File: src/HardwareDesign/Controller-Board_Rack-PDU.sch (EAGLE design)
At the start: 131 parts, among them IC2 RP2040, IC3 MCP6001, IC5 MIC5504-3.3YM5-TR, IC7 MP2315TSOT23-8, X1 25MHz, X2 12MHz

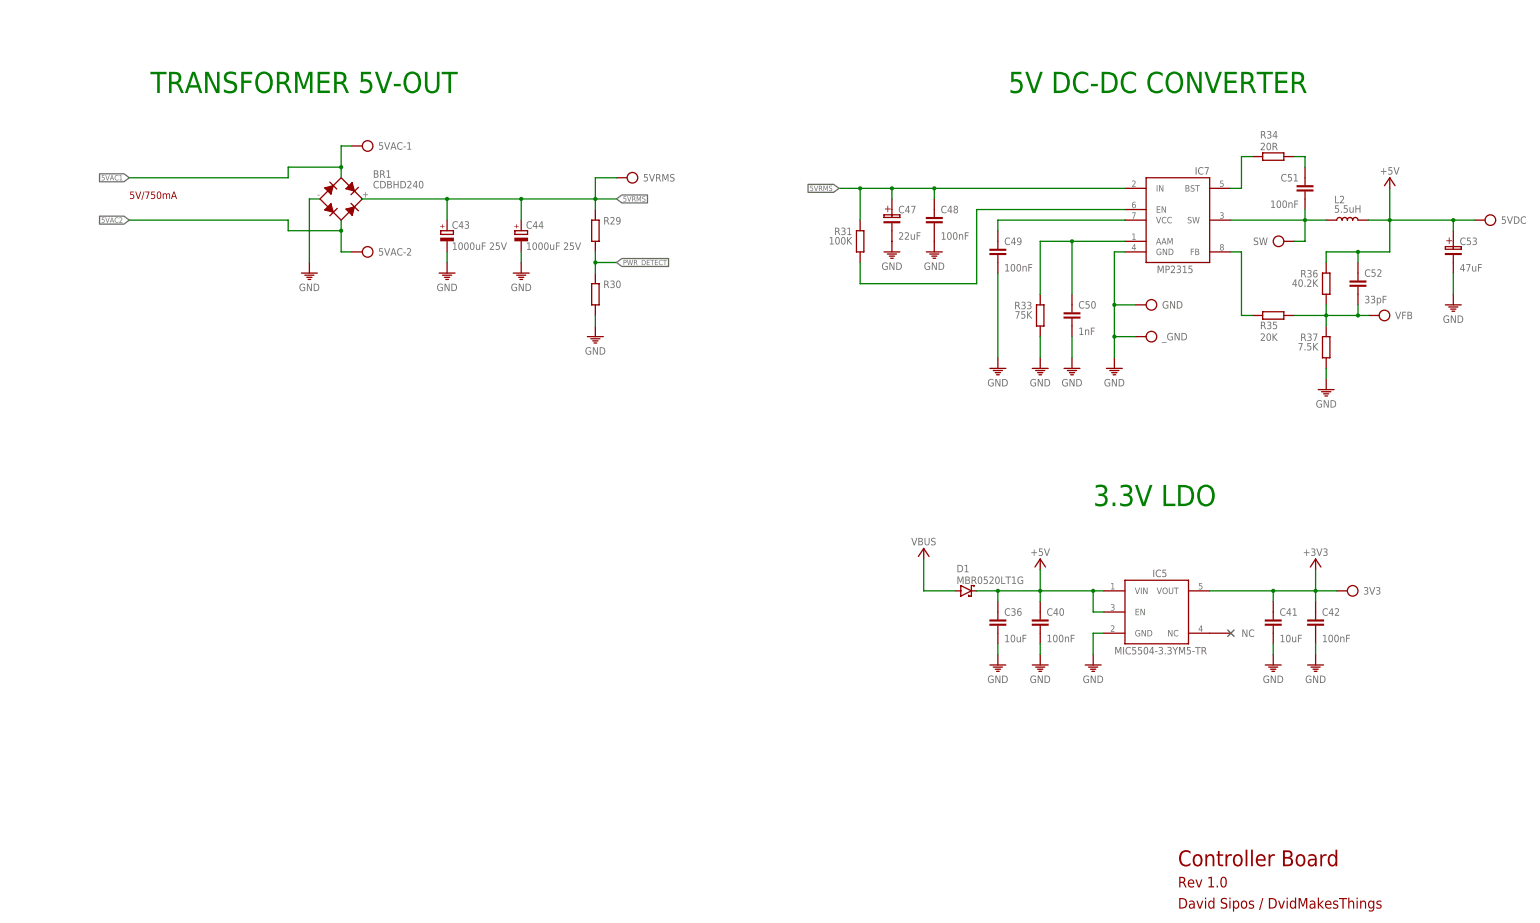
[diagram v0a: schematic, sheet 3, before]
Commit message: finish relay board design
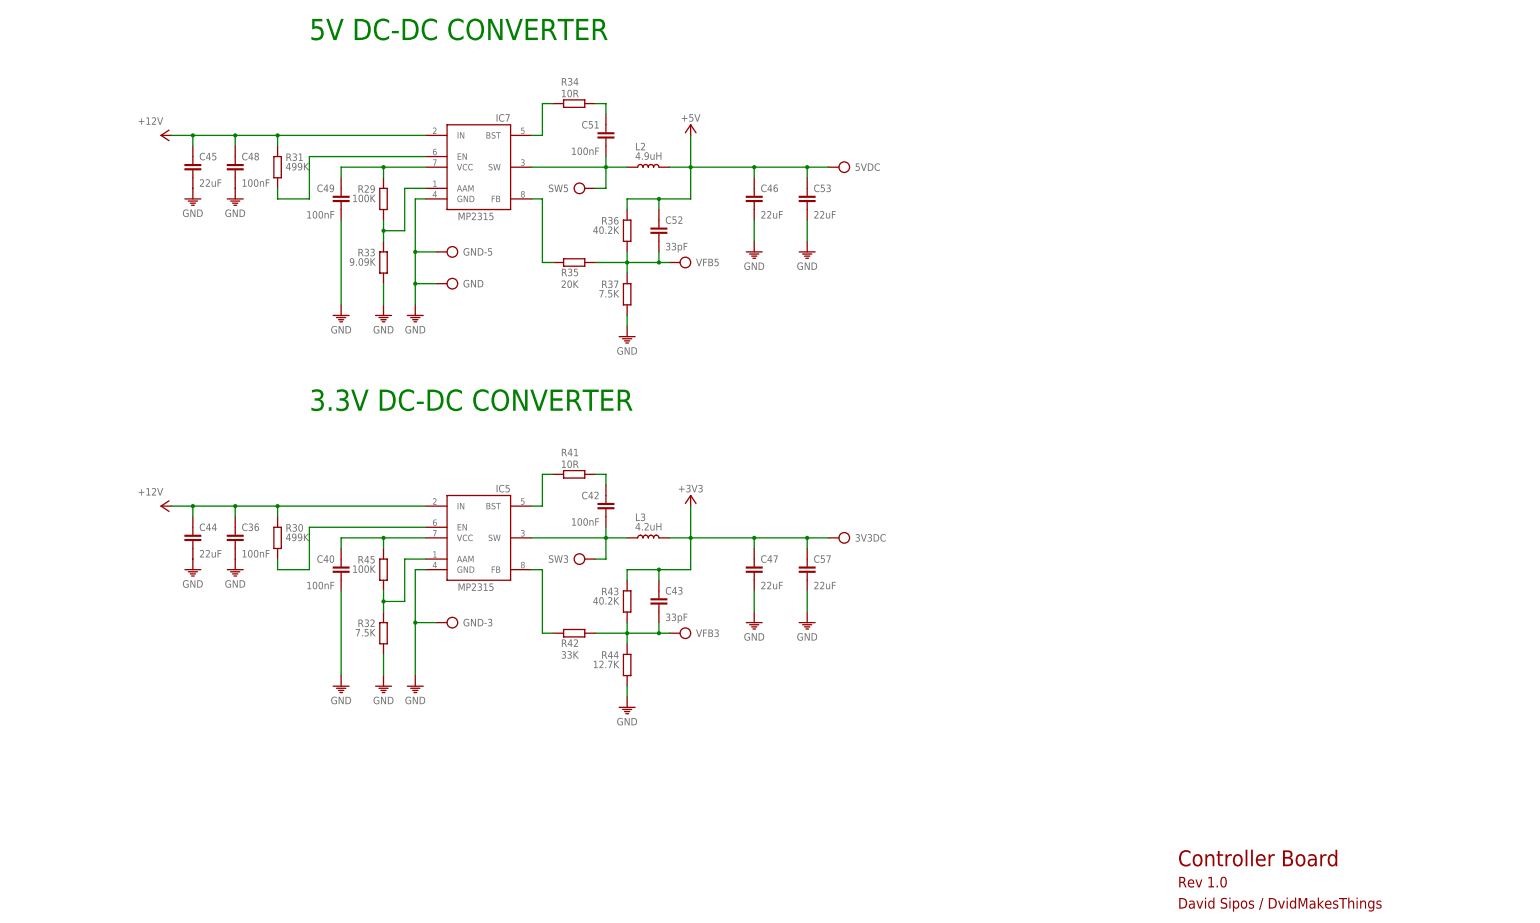
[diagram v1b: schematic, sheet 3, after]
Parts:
- removed 3V3, 5VAC-1, 5VAC-2, 5VRMS, SW, VFB, _GND: TP, ds_passive:TP
- removed BR1: CDBHD240, 52101-101-REV-A_v16:RECTIFIER_CDBHD240
- removed C41: 10uF, ds_passive:C0402
- removed C50: 1nF, ds_passive:C0402
- removed D1: MBR0520LT1G, Diodes:MBR0520LT1G
- added 12VFB, 3V3DC, GND-3, GND-5, SW3, SW5, VFB3, VFB5: TP, ds_passive:TP
- added C45, C46, C57: 22uF, ds_passive:C-1206
- added L3: 4.2uH, ds_passive:L
- added R32: 7.5K, ds_passive:R0402
- added R41: 10R, ds_passive:R0402
- added R42: 33K, ds_passive:R0402
- added R43: 40.2K, ds_passive:R0402
- added R44: 12.7K, ds_passive:R0402
- added R45: 100K, ds_passive:R0402
- added R46, R47: 0R, ds_passive:R0402
- added R48, R49: 4.7K, ds_passive:R0402
- added R50: 10K, ds_passive:R0402
- added RESET: B3U-1000P, 52101-101-REV-A_v16:SWITCH-OMRON_B3U-1000P
- C1, C10, C11, C12, C13, C14, C15, C16, C17, C18, C19, C2, C20, C21, C22, C23, C24, C25, C28, C29, C3, C30, C31, C32, C33, C34, C35, C37, C38, C39, C4, C55, C56, C6, C7, C8, C9: device ds_passive:C0402 -> ds_passive:C-0402
- C36: value 10uF -> 100nF
- C43: value 1000uF 25V -> 33pF; device Capacitor:C-POL_RADIAL-11MM-DIA -> ds_passive:C0402
- C44: value 1000uF 25V -> 22uF; device Capacitor:C-POL_RADIAL-11MM-DIA -> ds_passive:C-1206
- C47: device ds_passive:CPOL -> ds_passive:C-1206
- C5: device ds_passive:C1206 -> ds_passive:C-1206
- C53: value 47uF -> 22uF; device ds_passive:CPOL -> ds_passive:C-1206
- IC5: value MIC5504-3.3YM5-TR -> MP2315S; device ds_ic_vreg:MIC5504-3.3YM5-TR -> ds_ic_vreg:MP2315TSOT23-8
- IC7: value MP2315TSOT23-8 -> MP2315S
- L2: value 5.5uH -> 4.9uH
- R29: value (none) -> 100K; device ds_passive:R1206 -> ds_passive:R0402
- R30: value (none) -> 499K; device ds_passive:R1206 -> ds_passive:R0402
- R31: value 100K -> 499K
- R33: value 75K -> 9.09K
- R34: value 20R -> 10R
- R5, R6: device ds_passive:R0402 -> ds_passive:C-0402
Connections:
- removed net 12_VFB: IC2.GPIO27/ADC1, J1.3
- removed net 5VAC1: 5VAC-1.P$1, BR1.A1
- removed net 5VAC2: 5VAC-2.P$1, BR1.A2
- removed net 5VRMS: 5VRMS.P$1, BR1.+, C43.+, C44.+, C47.1, C48.1, IC7.IN, R29.1, R31.1
- removed net IAC: IC2.GPIO28/ADC2, J1.4
- removed net N$27: J2.12
- removed net N$28: J2.10
- removed net N$29: J2.8
- removed net N$30: J2.6
- removed net N$32: C50.1, IC7.AAM, R33.1
- new net +12V: C36.1, C44.1, C45.1, C48.1, IC5.IN, IC7.IN, J1.14, R30.1, R31.1, R48.2
- new net I_MEA/TX: IC2.GPIO28/ADC2, J1.4, R46.1
- new net N$11: IC5.BST, R41.2
- new net N$12: IC5.AAM, R32.1, R45.2
- new net N$13: IC7.AAM, R29.2, R33.1
- new net N$16: C49.1, IC7.VCC, R29.1
- new net N$17: IC2.RUN, R50.2, RESET.P
- new net N$20: IC5.FB, R42.1
- new net N$21: C42.2, IC5.SW, L3.1, SW3.P$1
- new net N$22: C42.1, R41.1
- new net N$24: C43.2, R42.2, R43.2, R44.1, VFB3.P$1
- new net N$26: IC5.EN, R30.2
- new net V_MEA/RX: IC2.GPIO27/ADC1, J1.3, R47.1
- net +3V3: now also 3V3DC.P$1, C43.1, C47.1, C57.1, L3.2, R43.1, R50.1; no longer 3V3.P$1, C41.1, C42.1, IC5.VOUT
- net +5V: now also C46.1; no longer C36.1, C40.1, D1.C, IC5.EN, IC5.VIN
- net GND: now also C44.2, C45.2, C46.2, C57.2, GND-3.P$1, GND-5.P$1, R32.2, R44.2, R49.1, RESET.S; no longer BR1.-, C41.2, C42.2, C43.-, C44.-, C50.2, J1.14, R30.2, _GND.P$1
- net N$31: now also C40.1, IC5.VCC, R45.1; no longer C49.1, IC7.VCC
- net N$35: now also SW5.P$1; no longer SW.P$1
- net N$37: now also VFB5.P$1; no longer VFB.P$1
- net PWR_DETECT: now also 12VFB.P$1, R48.1, R49.2; no longer R29.2, R30.1
- net UART0_RX: now also R47.2
- net UART0_TX: now also R46.2
- net VBUS: no longer D1.A
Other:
- note added: "3.3V DC-DC CONVERTER"
- note removed: "3.3V LDO"
- note removed: "5V/750mA"
- note removed: "TRANSFORMER 5V-OUT"
- moved on the sheet: 5VDC, C2, C36, C40, C42, C48, C49, C5, C51, C52, ETH1, GND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

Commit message: first order send to JLCPCB
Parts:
- C44, C45: value 22uF -> CL31A226KAHNNNE - 22uF 25V
- C46, C47, C53, C57: value 22uF -> CL31A226KPHNNNE - 22uF - 10V
- ESD1: value (none) -> SP0503BAHTG-ES
- IC1: value (none) -> W5500
- IC3: value MCP6001 -> MCP6001AIDBVRG
- IC4: value (none) -> W25Q128JVPIQ
- IC6: value (none) -> CAT24C256HU4IGT3
- IC7: value MP2315S -> MP2315GJ-Z
- IC8: value (none) -> MCP23S18-E/MJ
- R38: value 742C083103JP -> 4D03WGJ0332T5E
- RESET, USB_BOOT: value B3U-1000P -> B3U-1000P-B
- USBC: value 629722000214 -> USB-TYPE-C-018
- X1: value 25MHz -> RL250001791
- X2: value 12MHz -> SX3M12.000B10F20TNN
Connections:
- removed net N$10: IC8.GPB1
- removed net N$77: IC8.GPB0
- removed net N$78: IC8.GPB2
- removed net N$79: IC8.GPB3
- removed net N$80: IC8.GPB4
- removed net N$81: IC8.GPB5
- removed net N$82: IC8.GPB6
- removed net N$83: IC8.GPB7

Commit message: change X1, X2 because of shortage
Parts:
- X1: value RL250001791 -> XC53M4-25.000-F18NJDTL
- X2: value SX3M12.000B10F20TNN -> 5TJ412000UYGBC
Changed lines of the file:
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@@
 <part name="GND6" library="ds_passive" deviceset="GND" device=""/>
 <part name="GND7" library="ds_passive" deviceset="GND" device=""/>
-<part name="X1" library="ds_passive" deviceset="CRYSTAL" device="" package3d_urn="urn:adsk.eagle:package:16378248/1" value="RL250001791"/>
+<part name="X1" library="ds_passive" deviceset="CRYSTAL" device="" package3d_urn="urn:adsk.eagle:package:16378248/1" value="XC53M4-25.000-F18NJDTL "/>
 <part name="C8" library="ds_passive" deviceset="C" device="-0402" package3d_urn="urn:adsk.eagle:package:46766485/2" value="18pF"/>
 <part name="C9" library="ds_passive" deviceset="C" device="-0402" package3d_urn="urn:adsk.eagle:package:46766485/2" value="18pF"/>
@@
 <part name="FRAME2" library="frames" library_urn="urn:adsk.eagle:library:229" deviceset="A3L-LOC" device=""/>
 <part name="IC2" library="ds_ic_mcu" deviceset="RP2040" device="" package3d_urn="urn:adsk.eagle:package:6365073/1"/>
-<part name="X2" library="ds_passive" deviceset="CRYSTAL" device="" package3d_urn="urn:adsk.eagle:package:16378248/1" value="SX3M12.000B10F20TNN"/>
+<part name="X2" library="ds_passive" deviceset="CRYSTAL" device="" package3d_urn="urn:adsk.eagle:package:16378248/1" value="5TJ412000UYGBC "/>
 <part name="C19" library="ds_passive" deviceset="C" device="-0402" package3d_urn="urn:adsk.eagle:package:46766485/2" value="15pF"/>
 <part name="C20" library="ds_passive" deviceset="C" device="-0402" package3d_urn="urn:adsk.eagle:package:46766485/2" value="15pF"/>
@@
 <instance part="X2" gate="G$1" x="43.18" y="175.26" smashed="yes">
 <attribute name="NAME" x="38.1" y="178.435" size="1.778" layer="95"/>
-<attribute name="VALUE" x="38.1" y="165.1" size="1.778" layer="96"/>
+<attribute name="VALUE" x="33.02" y="165.1" size="1.778" layer="96"/>
 </instance>
 <instance part="C19" gate="G$1" x="27.94" y="165.1" smashed="yes" rot="MR0">
@@
 </instance>
 <instance part="X1" gate="G$1" x="38.1" y="193.04" smashed="yes">
-<attribute name="NAME" x="33.02" y="196.215" size="1.778" layer="95"/>
-<attribute name="VALUE" x="33.02" y="182.88" size="1.778" layer="96"/>
+<attribute name="NAME" x="35.56" y="182.245" size="1.778" layer="95" rot="R180"/>
+<attribute name="VALUE" x="53.34" y="198.12" size="1.778" layer="96" rot="R180"/>
 </instance>
 <instance part="C8" gate="G$1" x="22.86" y="182.88" smashed="yes" rot="MR0">

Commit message: update documentation
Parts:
- X1: value XC53M4-25.000-F18NJDTL -> XC53M4-25.000-F18NJDTL
- X2: value 5TJ412000UYGBC -> K5A1200015304P
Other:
- moved on the sheet: 3V3DC, 5VDC, C36, C40, C42, C43, C44, C45, C46, C47, C48, C49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

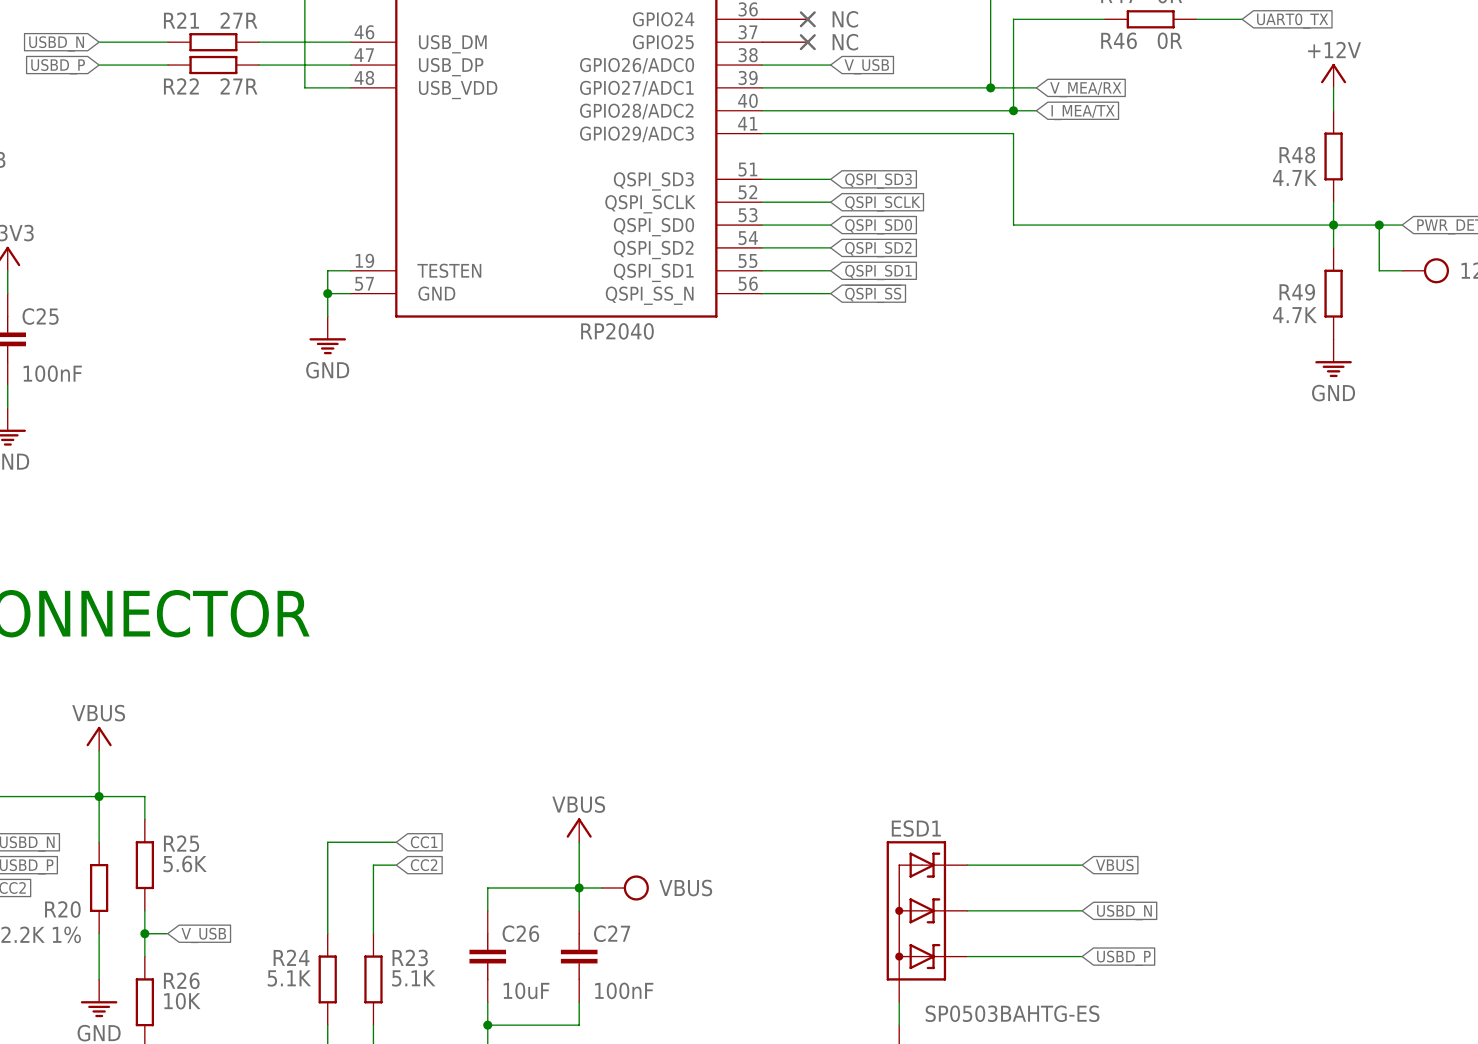
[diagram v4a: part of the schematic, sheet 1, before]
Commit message: correct wrong divider resistor values
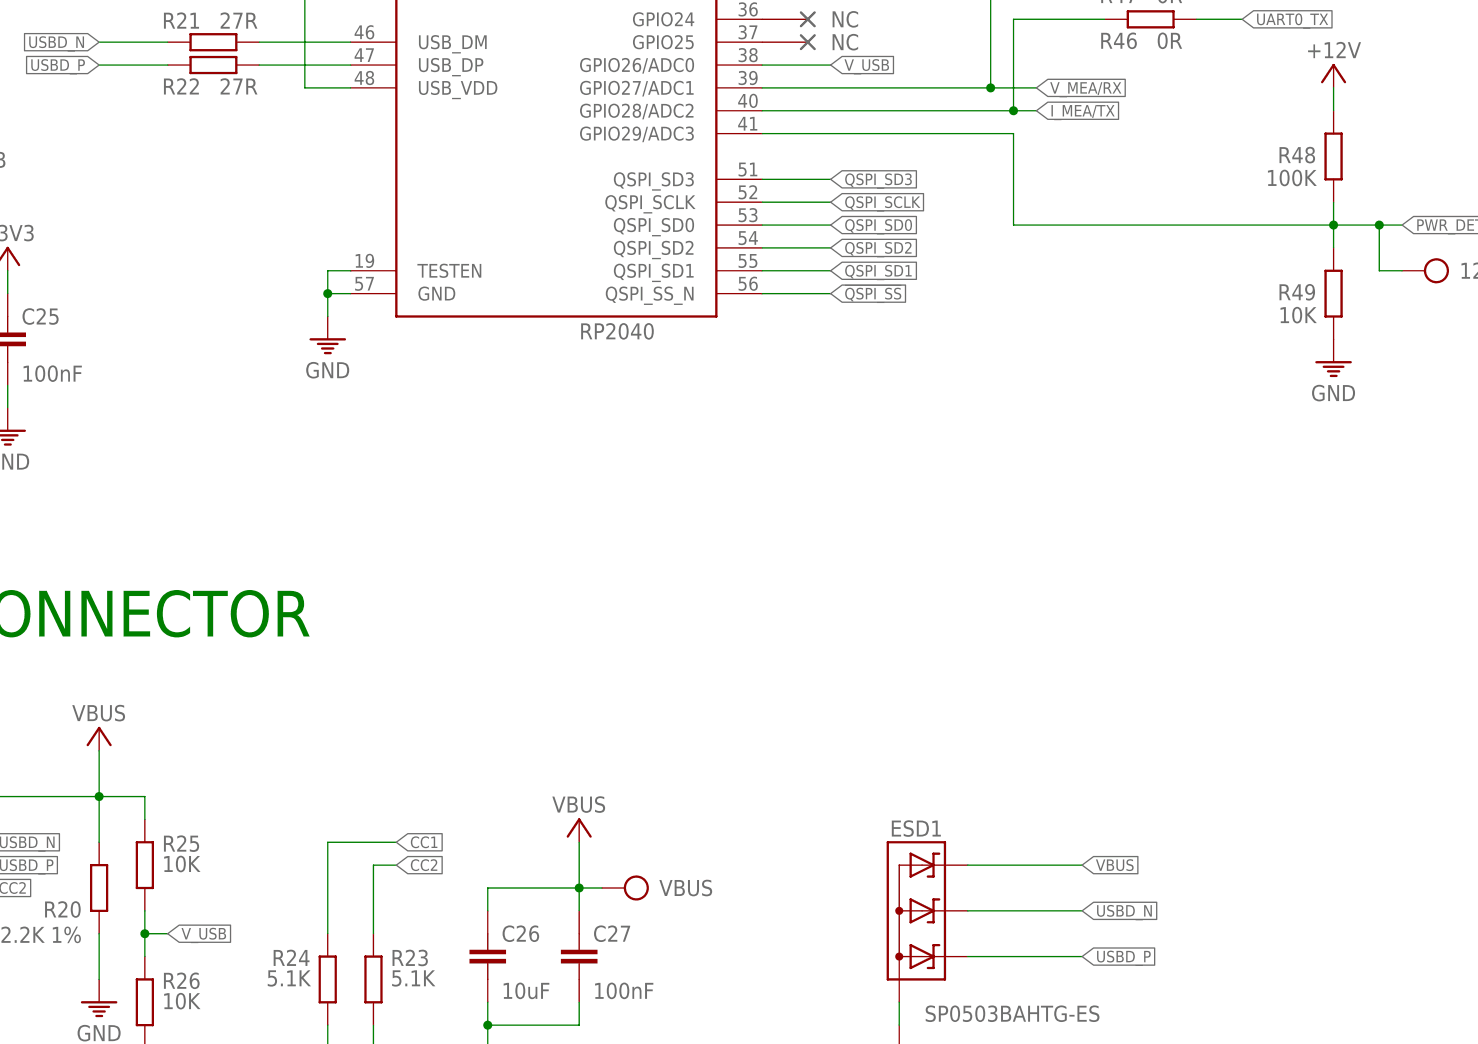
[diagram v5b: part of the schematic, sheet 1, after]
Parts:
- R25: value 5.6K -> 10K
- R48: value 4.7K -> 100K
- R49: value 4.7K -> 10K
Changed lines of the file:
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@@
 <part name="DBG2" library="ds_con" deviceset="CON-1X4" device="" package3d_urn="urn:adsk.eagle:package:46684991/2"/>
 <part name="GND38" library="ds_passive" deviceset="GND" device=""/>
-<part name="R25" library="ds_passive" library_urn="urn:adsk.eagle:library:46685041" deviceset="R" device="0402" package3d_urn="urn:adsk.eagle:package:46683744/2" value="5.6K"/>
+<part name="R25" library="ds_passive" library_urn="urn:adsk.eagle:library:46685041" deviceset="R" device="0402" package3d_urn="urn:adsk.eagle:package:46683744/2" value="10K"/>
 <part name="R26" library="ds_passive" library_urn="urn:adsk.eagle:library:46685041" deviceset="R" device="0402" package3d_urn="urn:adsk.eagle:package:46683744/2" value="10K"/>
 <part name="GND39" library="ds_passive" library_urn="urn:adsk.eagle:library:46685041" deviceset="GND" device=""/>
@@
 <part name="NC15" library="ds_passive" deviceset="NC" device=""/>
 <part name="NC18" library="ds_passive" deviceset="NC" device=""/>
-<part name="R48" library="ds_passive" deviceset="R" device="0402" package3d_urn="urn:adsk.eagle:package:46683744/2" value="4.7K"/>
-<part name="R49" library="ds_passive" deviceset="R" device="0402" package3d_urn="urn:adsk.eagle:package:46683744/2" value="4.7K"/>
+<part name="R48" library="ds_passive" deviceset="R" device="0402" package3d_urn="urn:adsk.eagle:package:46683744/2" value="100K"/>
+<part name="R49" library="ds_passive" deviceset="R" device="0402" package3d_urn="urn:adsk.eagle:package:46683744/2" value="10K"/>
 <part name="GND47" library="ds_passive" deviceset="GND" device=""/>
 <part name="P+8" library="ds_passive" deviceset="+12V" device=""/>
